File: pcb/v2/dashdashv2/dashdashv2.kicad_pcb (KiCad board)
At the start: 2 copper layers, 69 parts, among them J1 USB_B, J2 Tag connect, J3 Conn_01x04_Female, Q1 IRF540N, Q2 IRF540N, Q3 2N3904, U1 RP2040, U10 PCA9685PW, U11 MIC2940A-3.3WU, U13 LT4363IMS, U14 ADUM4160, U2 W25Q128JVS, U3 MCP2515-xSO, U4 TJA1042T3118, U7 25LCxxx, U9 MIC2940A-5.0WT, Y1 12MHz, Y2 12MHz

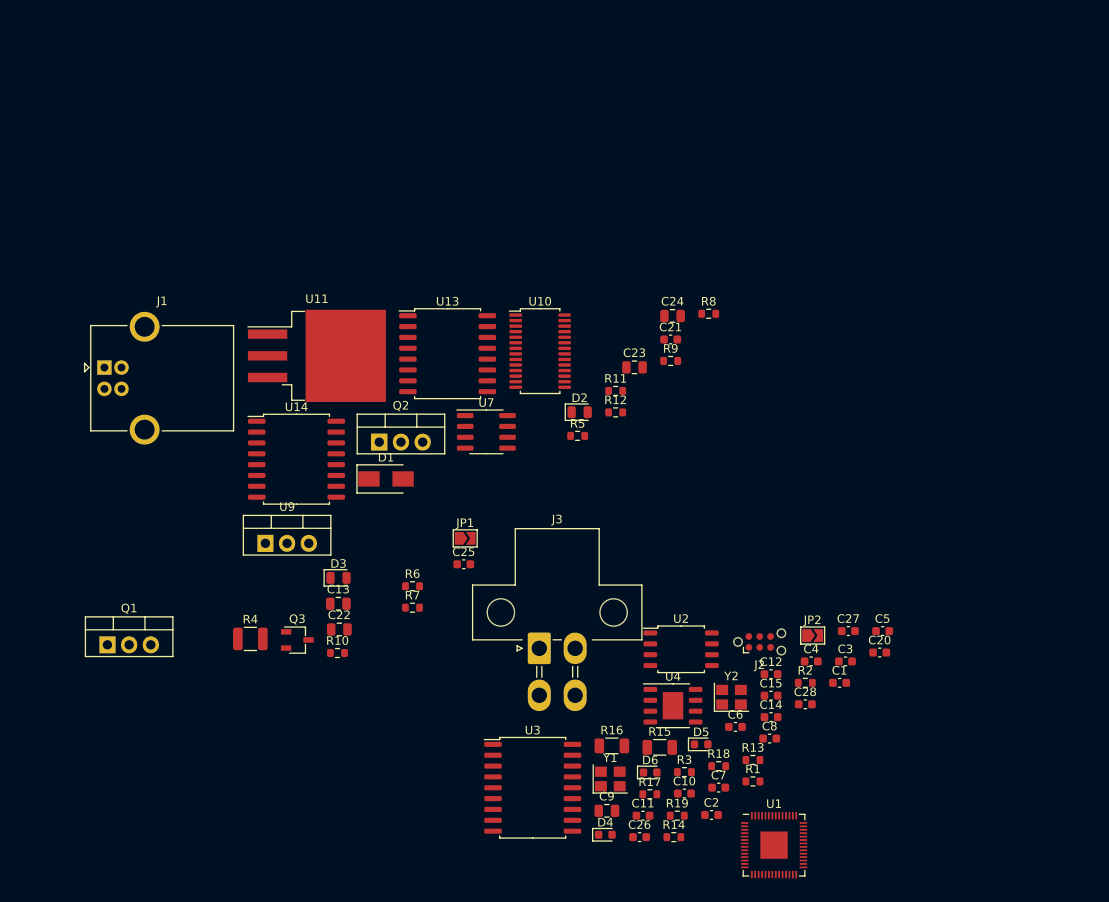
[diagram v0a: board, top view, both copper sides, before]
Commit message: ESD SPI
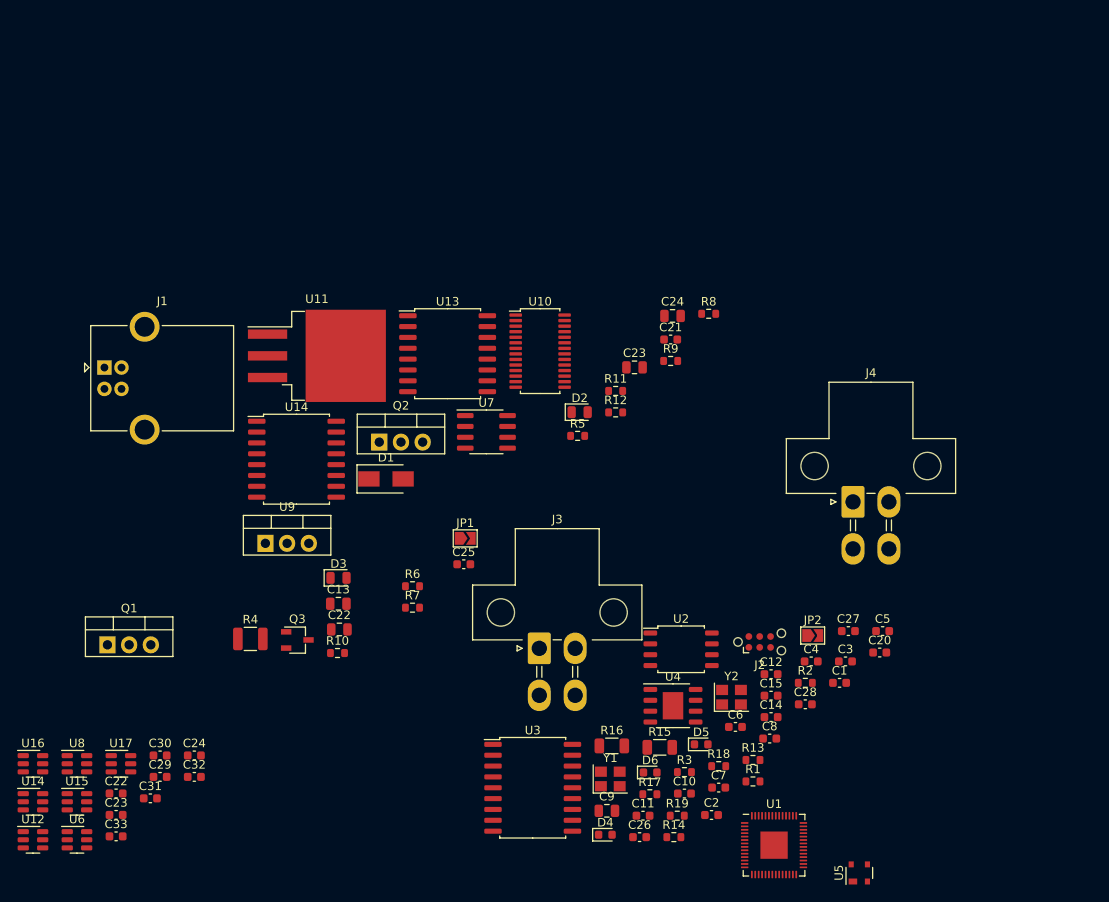
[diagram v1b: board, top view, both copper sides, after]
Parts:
- added C22: 100nF, Capacitor_SMD:C_0603_1608Metric, F.Cu at (110.0, 117.8)
- added C23: 100nF, Capacitor_SMD:C_0603_1608Metric, F.Cu at (110.0, 120.3)
- added C24: 100nF, Capacitor_SMD:C_0603_1608Metric, F.Cu at (119.2, 113.3)
- added C29: 100nF, Capacitor_SMD:C_0603_1608Metric, F.Cu at (115.2, 115.8)
- added C30: 100nF, Capacitor_SMD:C_0603_1608Metric, F.Cu at (115.2, 113.3)
- added C31: 100nF, Capacitor_SMD:C_0603_1608Metric, F.Cu at (114.0, 118.3)
- added C32: 100nF, Capacitor_SMD:C_0603_1608Metric, F.Cu at (119.2, 115.8)
- added C33: 100nF, Capacitor_SMD:C_0603_1608Metric, F.Cu at (110.0, 122.8)
- added J4: Conn_01x04_Female, Connector_Molex:Molex_Mini-Fit_Jr_5569-04A1_2x02_P4.20mm_Horizontal, F.Cu at (196.3, 83.6)
- added U12: SRV05-4, Package_TO_SOT_SMD:SOT-23-6, F.Cu at (100.3, 123.2)
- added U14: SRV05-4, Package_TO_SOT_SMD:SOT-23-6, F.Cu at (100.3, 118.7)
- added U15: SRV05-4, Package_TO_SOT_SMD:SOT-23-6, F.Cu at (105.4, 118.7)
- added U16: SRV05-4, Package_TO_SOT_SMD:SOT-23-6, F.Cu at (100.3, 114.3)
- added U17: SRV05-4, Package_TO_SOT_SMD:SOT-23-6, F.Cu at (110.6, 114.3)
- added U5: TPD2E2U06, Package_TO_SOT_SMD:SOT-143, F.Cu at (197.0, 127.1)
- added U6: SRV05-4, Package_TO_SOT_SMD:SOT-23-6, F.Cu at (105.4, 123.2)
- added U8: SRV05-4, Package_TO_SOT_SMD:SOT-23-6, F.Cu at (105.4, 114.3)
- R10, R11: value R_Small -> 22r
- Y1: value 12MHz -> 8MHz
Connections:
- C28 pad 1: +1V1 -> unconnected-(C28-Pad1)
- C5 pad 2: Net-(C5-Pad2) -> /xin
- C6 pad 2: Net-(C6-Pad2) -> /xout
- J1 pad 1: Net-(C22-Pad1) -> Net-(J1-Pad1)
- J1 pad 2: /d- -> /USB_D-
- J1 pad 3: /d+ -> /USB_D+
- J1 pad 4: GND1 -> GND
- J1 pad 5: GND1 -> GND
- J3 pad 1: unconnected-(J3-Pad1) -> GND
- J3 pad 3: unconnected-(J3-Pad3) -> CAN-
- J3 pad 4: unconnected-(J3-Pad4) -> CAN+
- R1 pad 2: /USB_DM -> /USB_D-
- R2 pad 1: /USB_DP -> /USB_D+
- U1 pad 11: /GPIO8 -> unconnected-(U1-Pad11)
- U1 pad 12: /OLED_SDA -> /CLK2
- U1 pad 13: /OLED_SCL -> /MISO2
- U1 pad 14: /MODE_CHG -> /MOSI2
- U1 pad 15: unconnected-(U1-Pad15) -> /CS_CAN
- U1 pad 16: /CF_CONF0 -> unconnected-(U1-Pad16)
- U1 pad 17: /CF_CONF1 -> unconnected-(U1-Pad17)
- U1 pad 18: /CF_CONF2 -> unconnected-(U1-Pad18)
- U1 pad 2: /GPIO0 -> unconnected-(U1-Pad2)
- U1 pad 20: Net-(C5-Pad2) -> /xin
- U1 pad 21: Net-(C6-Pad2) -> /xout
- U1 pad 3: /GPIO1 -> unconnected-(U1-Pad3)
- U1 pad 30: /heater_pwm -> /CLK
- U1 pad 31: /D_SCL -> /MISO
- U1 pad 32: /D_SDA -> /MOSI
- U1 pad 35: /LSU_Vm -> /I2C1_SCL
- U1 pad 36: /Ip_dac -> /I2C1_SDA
- U1 pad 39: /Vm -> unconnected-(U1-Pad39)
- U1 pad 4: /GPIO2 -> unconnected-(U1-Pad4)
- U1 pad 40: /Ip_sense -> unconnected-(U1-Pad40)
- U1 pad 41: /UN_SENSE -> unconnected-(U1-Pad41)
- U1 pad 5: /GPIO3 -> unconnected-(U1-Pad5)
- U1 pad 6: /GPIO4 -> unconnected-(U1-Pad6)
- U1 pad 7: /GPIO5 -> unconnected-(U1-Pad7)
- U1 pad 8: /GPIO6 -> unconnected-(U1-Pad8)
- U1 pad 9: /GPIO7 -> unconnected-(U1-Pad9)
- U10 pad 10: /PWM_BAR3 -> /PWM_FUEL2
- U10 pad 11: /PWM_VEL -> /PWM_BAR1
- U10 pad 12: /PWM_OD -> /PWM_BAR2
- U10 pad 13: /PWM_BACK_1 -> /PWM_BAR3
- U10 pad 15: /PWM_BACK_2 -> /PWM_VEL
- U10 pad 16: unconnected-(U10-Pad16) -> /PWM_OD
- U10 pad 17: unconnected-(U10-Pad17) -> /PWM_BACK_1
- U10 pad 18: unconnected-(U10-Pad18) -> /PWM_BACK_2
- U10 pad 6: /PWM_FUEL1 -> /PWM_BACK_RPM
- U10 pad 7: /PWM_FUEL2 -> /PWM_SPEED1
- U10 pad 8: /PWM_BAR1 -> /PWM_SPEED2
- U10 pad 9: /PWM_BAR2 -> /PWM_FUEL1
- U3 pad 13: /GPIO0 -> /CLK2
- U3 pad 14: /GPIO1 -> /MISO2
- U3 pad 15: /GPIO2 -> /MOSI2
- U3 pad 16: /GPIO8 -> /CS_CAN
- Y2 pad 1: Net-(C6-Pad2) -> GND
- Y2 pad 2: GND -> /xin
- Y2 pad 3: Net-(C5-Pad2) -> GND
- Y2 pad 4: GND -> /xout

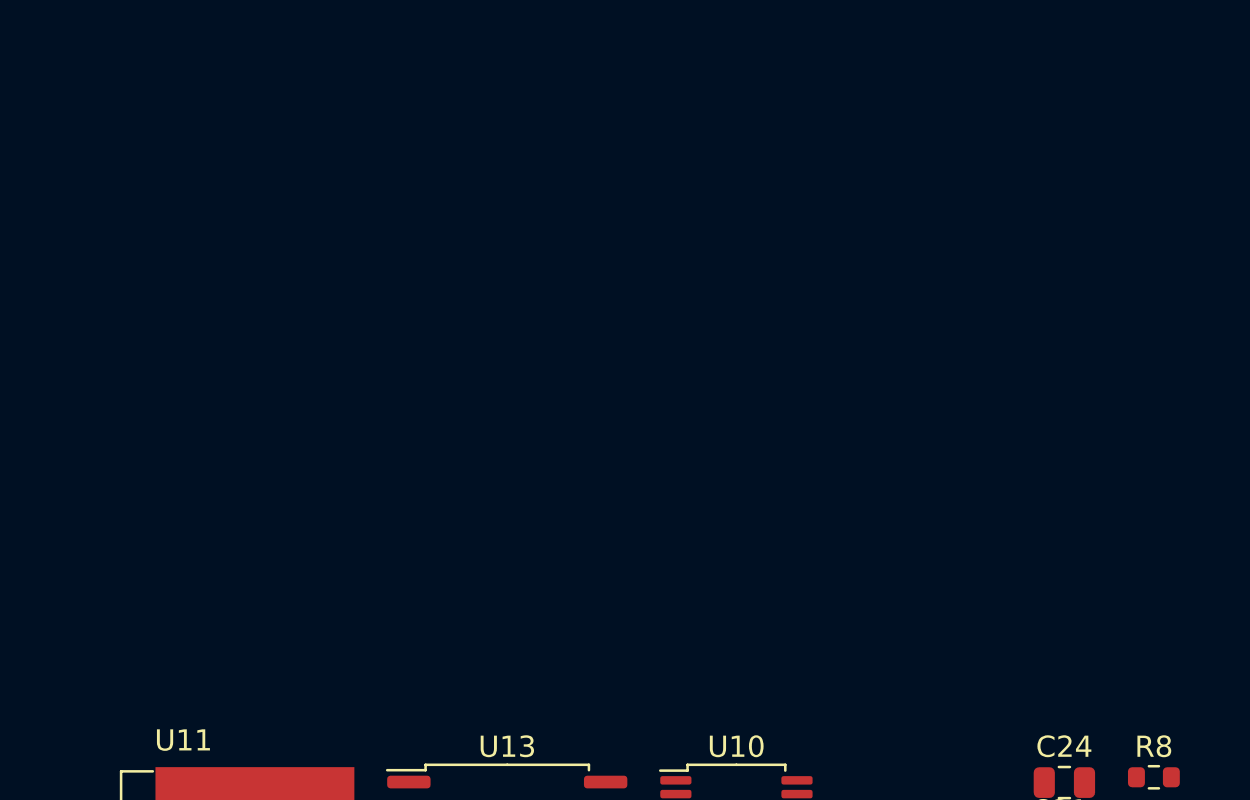
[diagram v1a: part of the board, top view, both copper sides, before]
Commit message: Add external modules connector
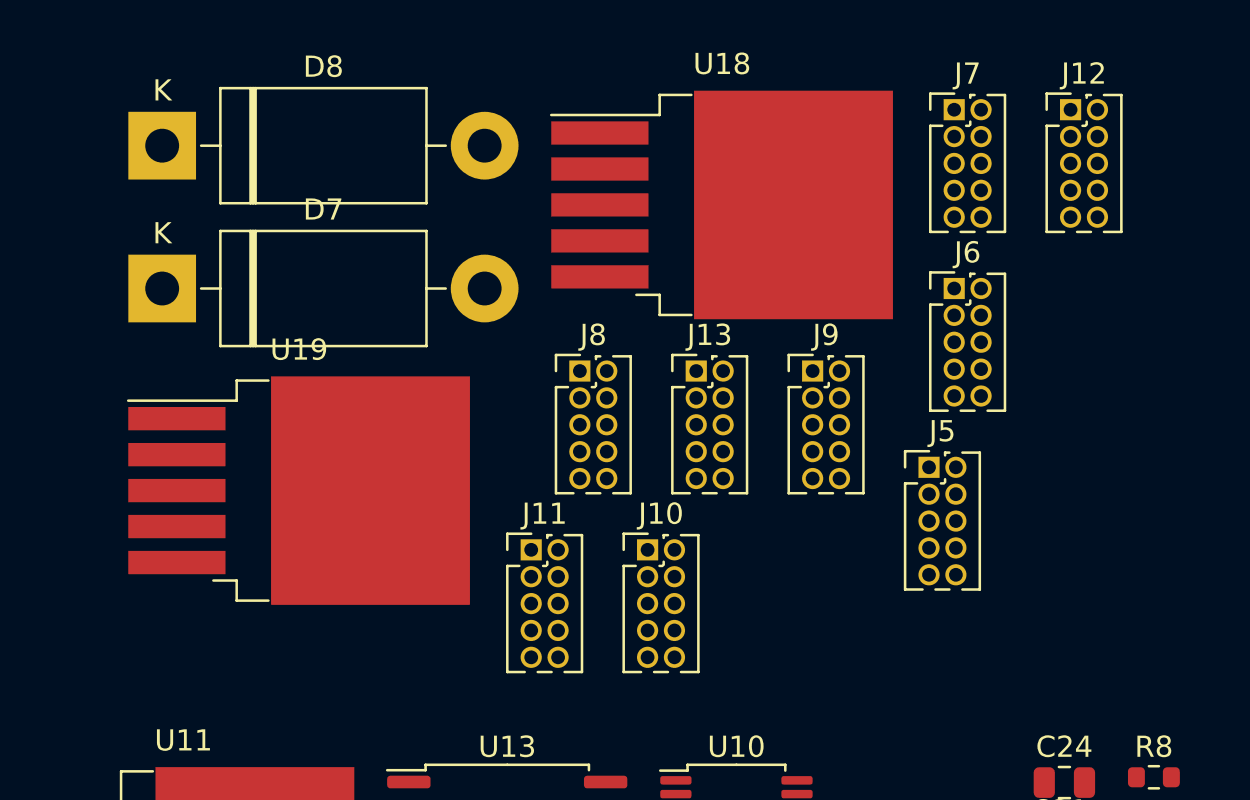
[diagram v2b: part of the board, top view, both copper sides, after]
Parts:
- added D7: 1N5822, Diode_THT:D_DO-201AD_P15.24mm_Horizontal, F.Cu at (132.5, 38.5)
- added D8: 1N5822, Diode_THT:D_DO-201AD_P15.24mm_Horizontal, F.Cu at (132.5, 31.8)
- added J10: O2_CONN1, Connector_PinHeader_1.27mm:PinHeader_2x05_P1.27mm_Vertical, F.Cu at (155.4, 50.9)
- added J11: BATT_CONN1, Connector_PinHeader_1.27mm:PinHeader_2x05_P1.27mm_Vertical, F.Cu at (149.9, 50.9)
- added J12: OIL_CONN1, Connector_PinHeader_1.27mm:PinHeader_2x05_P1.27mm_Vertical, F.Cu at (175.4, 30.1)
- added J13: OIL_TEMP1, Connector_PinHeader_1.27mm:PinHeader_2x05_P1.27mm_Vertical, F.Cu at (157.7, 42.4)
- added J5: SPEED_CONN1, Connector_PinHeader_1.27mm:PinHeader_2x05_P1.27mm_Vertical, F.Cu at (168.7, 47.0)
- added J6: DISPLAY1, Connector_PinHeader_1.27mm:PinHeader_2x05_P1.27mm_Vertical, F.Cu at (169.9, 38.5)
- added J7: RPM_CONN1, Connector_PinHeader_1.27mm:PinHeader_2x05_P1.27mm_Vertical, F.Cu at (169.9, 30.1)
- added J8: TEMP1, Connector_PinHeader_1.27mm:PinHeader_2x05_P1.27mm_Vertical, F.Cu at (152.2, 42.4)
- added J9: FUEL_CONN1, Connector_PinHeader_1.27mm:PinHeader_2x05_P1.27mm_Vertical, F.Cu at (163.2, 42.4)
- added U18: GL2576-3.3TA5R, Package_TO_SOT_SMD:TO-263-5_TabPin3, F.Cu at (159.0, 34.5)
- added U19: GL2576-5.0TA5R, Package_TO_SOT_SMD:TO-263-5_TabPin3, F.Cu at (139.0, 48.0)
